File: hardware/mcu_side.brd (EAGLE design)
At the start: 16.5 x 50 mm, 31 parts, among them CON1 JST-ZR-06, Q1 BSS138LT3G, U1 STM32F031G6U6

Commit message: Add start module
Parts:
- added SM_3.3V, SM_GND, SM_KILL, SM_START: PAD-SMD-ROUND-1.27PAD, Isaks Bibliotek:PAD.03X.05
- moved RPUP1 9.73 mm to (4.17, 3.91), flipped to the bottom
- moved RPUP2 4.89 mm to (7.82, 3.86), flipped to the bottom, turned to 90 degrees
- moved CON1 0.15 mm to (15.2, 44.6)
- moved TOF3 0.10 mm to (9.58, 4.60)
- moved TOF2 0.08 mm to (5.94, 4.60)
- moved TOF5 0.08 mm to (5.94, 13.8)
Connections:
- new net KILL: SM_KILL.P$1, U1.9
- new net START: SM_START.P$1, U1.8
- net 3.3V: now also SM_3.3V.P$1
- net GND: now also SM_GND.P$1
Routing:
- net KILL: track 0.00 -> 40.4 mm, vias 0 -> 2
- net START: track 0.00 -> 37.2 mm, vias 0 -> 2
- net SDA: track 46.5 -> 37.4 mm, vias 3 -> 1
- net 3.3V: track 114.6 -> 107.5 mm, vias 6 -> 8
- net STEER_PWM: track 30.0 -> 32.3 mm
- net GND: track 99.9 -> 102.2 mm, vias 5 -> 18
- net MOTOR_PWM: track 25.0 -> 26.0 mm
- net MOTOR_DIR: track 26.3 -> 27.3 mm
- net STEER_DIR: track 27.0 -> 28.0 mm
- net SCL: track 36.2 -> 35.3 mm
- net !XSHUT4: track 5.36 -> 6.19 mm
- net !XSHUT5: track 5.20 -> 5.93 mm
- added copper zone on layer 16, net GND
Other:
- board text added: "!XST"
- board text added: "+"
- board text added: "-"
- board text added: "3.3V"
- board text added: "C"
- board text added: "D"
- board text added: "DEBUG"
- board text added: "Donatello"
- board text added: "FB"
- board text added: "GND"
- board text added: "I2C Pullup"
- board text added: "K"
- board text added: "M_DIR"
- board text added: "M_PWM"
- board text added: "S"
- board text added: "SCL"
- board text added: "SDA"
- board text added: "STATUS"
- board text added: "S_DIR"
- board text added: "S_PWM"
- board text added: "VIN"

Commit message: Logo and name on tPlace/bPlace
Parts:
- moved RFBB 1.00 mm to (9.73, 44.7)
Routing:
- net N$3: track 8.63 -> 9.71 mm
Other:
- board text added: "C:/Users/Isak/Downloads/Donatello_rotated.bmp"
- board text added: "MCU SIDE"
- board text removed: "Donatello"

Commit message: Production ready
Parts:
- added ENC_3.3V, ENC_A, ENC_B, ENC_GND: PAD-SMD-ROUND-1.27PAD, Isaks Bibliotek:PAD.03X.05
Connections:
- new net ENC_A: ENC_A.P$1, U1.25
- new net ENC_B: ENC_B.P$1, U1.26
- net 3.3V: now also ENC_3.3V.P$1
- net GND: now also ENC_GND.P$1
- net MOTOR_DIR: now also U1.27; no longer U1.26
- net STEER_DIR: now also U1.28; no longer U1.25
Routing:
- net ENC_B: track 0.00 -> 35.3 mm, vias 0 -> 1
- net ENC_A: track 0.00 -> 29.4 mm, vias 0 -> 1
- net GND: track 102.1 -> 106.3 mm
- net 3.3V: track 107.3 -> 110.2 mm, vias 8 -> 9
- net SDA: track 37.4 -> 39.4 mm
- net START: track 37.2 -> 38.9 mm
- net VOLTM: track 36.8 -> 38.4 mm
- net !RESET: track 17.8 -> 19.2 mm
- net SCL: track 35.3 -> 36.6 mm
- net STEER_DIR: track 28.0 -> 28.8 mm
- net SWCLK: track 4.13 -> 4.69 mm
- net MOTOR_DIR: track 27.3 -> 27.9 mm
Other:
- board text added: "A"
- board text added: "B"

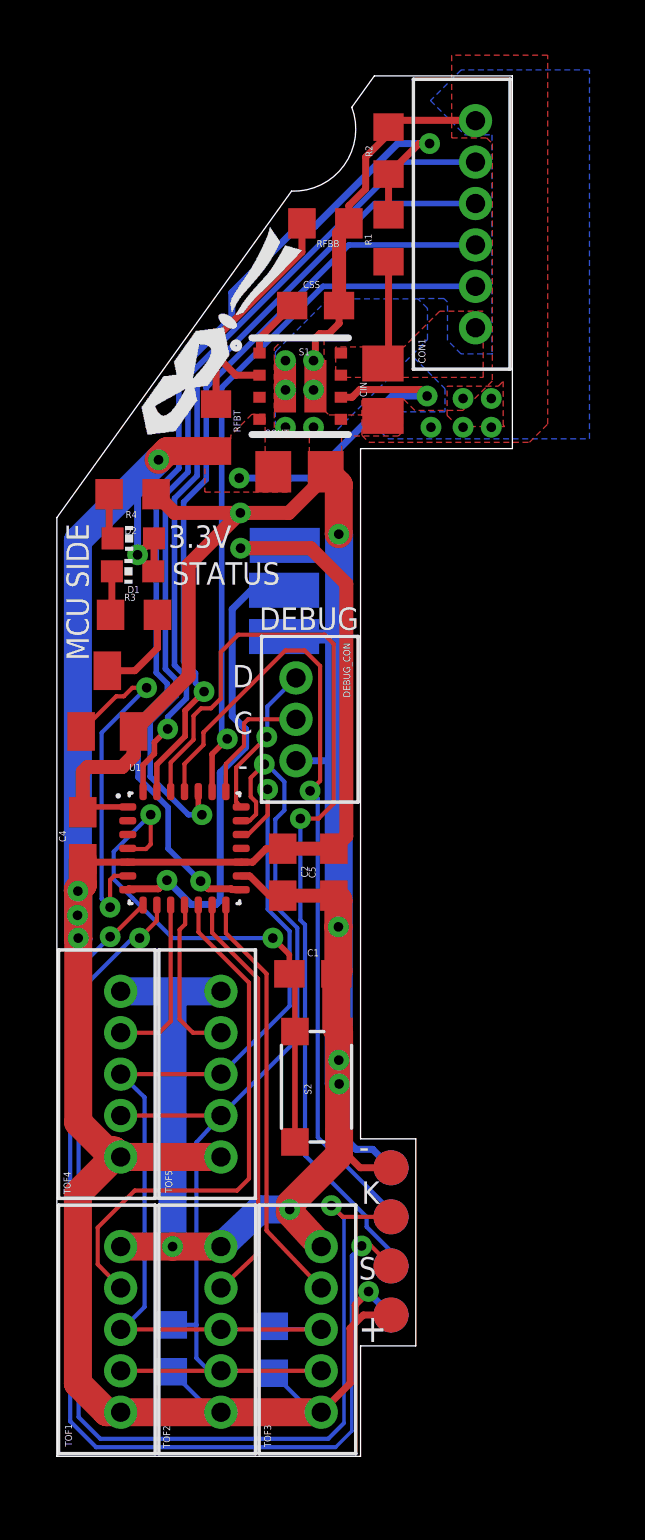
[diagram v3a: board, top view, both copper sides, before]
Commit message: VReg changed to linear LM1117, 3.3V
The switching VREG burned the MCU twice..... Switched to an old classic :)
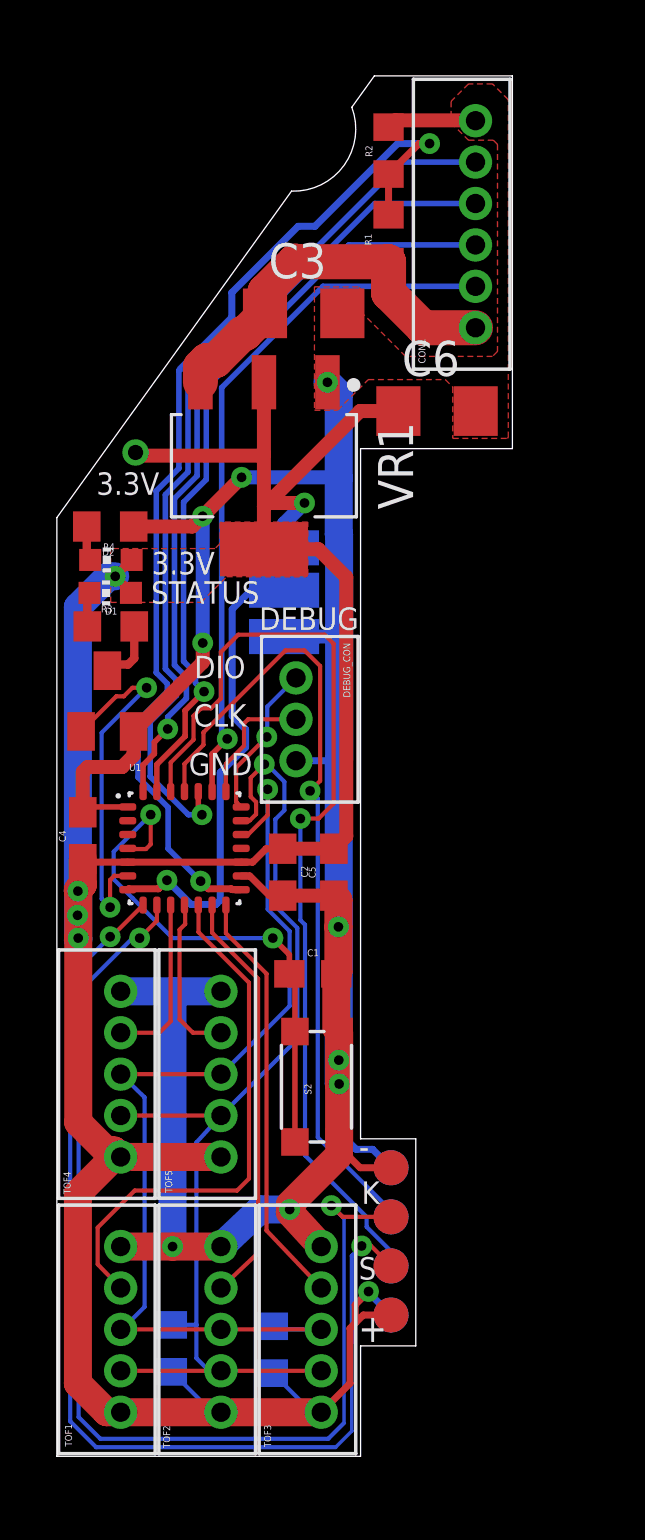
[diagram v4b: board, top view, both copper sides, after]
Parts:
- removed CIN, COUT: 10u, CASE-RCL:C0805
- removed CSS: 3300p, CASE-RCL:C0603
- removed RFBB: 380k, CASE-RCL:R0603
- removed RFBT: 1.2M, CASE-RCL:R0603
- removed S1: LMZ21701, Isaks Bibliotek:LMZ21701
- added C3, C6: 10u, CASE-RCL:C1206
- added VR1: LM1117-3.3, Isaks Bibliotek:SOT230P700X180-4
- moved R4 1.42 mm to (1.93, 33.7)
- moved D2 1.12 mm to (1.96, 32.5)
- moved D1 1.12 mm to (1.93, 31.3)
- moved R3 0.94 mm to (1.95, 30.1)
- moved FB+ 0.09 mm to (8.22, 32.9)
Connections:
- removed net N$1: CSS.1, S1.1
- removed net N$3: RFBB.1, RFBT.1, S1.2
- net 3.3V: now also C6.1, VR1.2, VR1.4; no longer COUT.1, RFBT.2, S1.4, S1.6
- net GND: now also C3.2, C6.2, VR1.1; no longer CIN.2, COUT.2, CSS.2, RFBB.2, S1.10, S1.5, S1.9
- net VIN: now also C3.1, VR1.3; no longer CIN.1, S1.7, S1.8
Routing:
- net VIN: track 3.77 -> 14.2 mm
- net N$3: track 9.71 -> 0.00 mm
- net GND: track 106.3 -> 99.2 mm, vias 18 -> 9
- net 3.3V: track 110.2 -> 106.2 mm, vias 9 -> 7
- net N$1: track 2.21 -> 0.00 mm
- net N$17: track 3.36 -> 2.32 mm
- removed copper zone on layer 16, net GND
- removed copper zone on layer 1, net VIN
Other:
- board text added: "CLK"
- board text added: "DIO"
- board text removed: "C"
- board text removed: "D"
- board text removed: "MCU SIDE"
